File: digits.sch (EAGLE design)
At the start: 49 parts, among them IC1 STP16CP05 / STP16CPC26, IC2 STP16CP05 / STP16CPC26, IC3 ATMEGA32U4QFN, IC4 ATMEGA32U4TQFP-44, J1 POWER_JACKPTH_LOCK, J2 ACCESSORY, X1 CRYSTALHC49

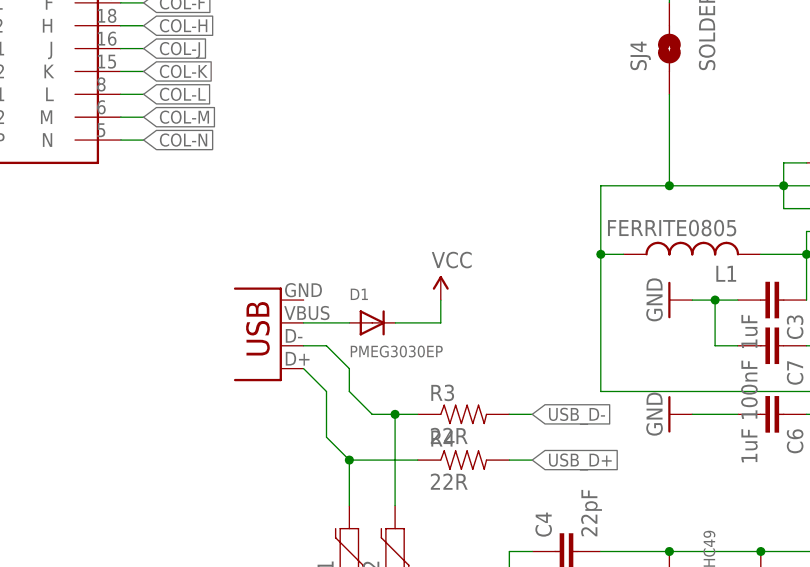
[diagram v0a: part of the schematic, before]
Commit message: grounded usb (fixes #3)
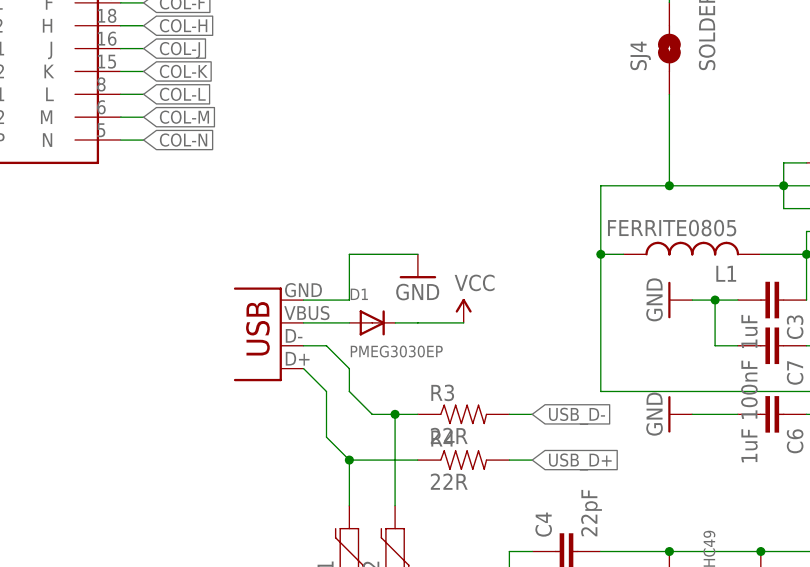
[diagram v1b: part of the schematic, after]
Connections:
- net GND: now also JP2.GND
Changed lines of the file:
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@@
 <attribute name="PARTNO" value="PMEG3030EP-115"/>
 </part>
+<part name="GND17" library="SparkFun-Aesthetics" deviceset="GND" device=""/>
 </parts>
 <sheets>
@@
 <attribute name="PARTNO" x="246.38" y="43.18" size="1.778" layer="96" display="off"/>
 </instance>
-<instance part="SUPPLY3" gate="G$1" x="254" y="45.72"/>
+<instance part="SUPPLY3" gate="G$1" x="256.54" y="43.18"/>
 <instance part="JP3" gate="G$1" x="12.7" y="38.1">
 <attribute name="PARTNO" x="12.7" y="38.1" size="1.778" layer="96" display="off"/>
@@
 <attribute name="PARTNO" x="281.94" y="-40.64" size="1.778" layer="96" display="off"/>
 </instance>
+<instance part="GND17" gate="1" x="251.46" y="48.26"/>
 </instances>
 <busses>
@@
 <pinref part="D1" gate="G$1" pin="C"/>
 <pinref part="SUPPLY3" gate="G$1" pin="VCC"/>
-<wire x1="248.92" y1="43.18" x2="254" y2="43.18" width="0.1524" layer="91"/>
-<wire x1="254" y1="43.18" x2="254" y2="45.72" width="0.1524" layer="91"/>
+<wire x1="248.92" y1="43.18" x2="251.46" y2="43.18" width="0.1524" layer="91"/>
+<wire x1="251.46" y1="43.18" x2="256.54" y2="43.18" width="0.1524" layer="91"/>
 </segment>
 <segment>
@@
 <label x="63.5" y="33.02" size="1.4224" layer="95" xref="yes"/>
 </segment>
-</net>
+<segment>
+<pinref part="JP2" gate="G$1" pin="GND"/>
+<wire x1="238.76" y1="45.72" x2="243.84" y2="45.72" width="0.1524" layer="91"/>
+<wire x1="243.84" y1="45.72" x2="243.84" y2="50.8" width="0.1524" layer="91"/>
+<pinref part="GND17" gate="1" pin="GND"/>
+<wire x1="243.84" y1="50.8" x2="251.46" y2="50.8" width="0.1524" layer="91"/>
+</segment>
+</net>

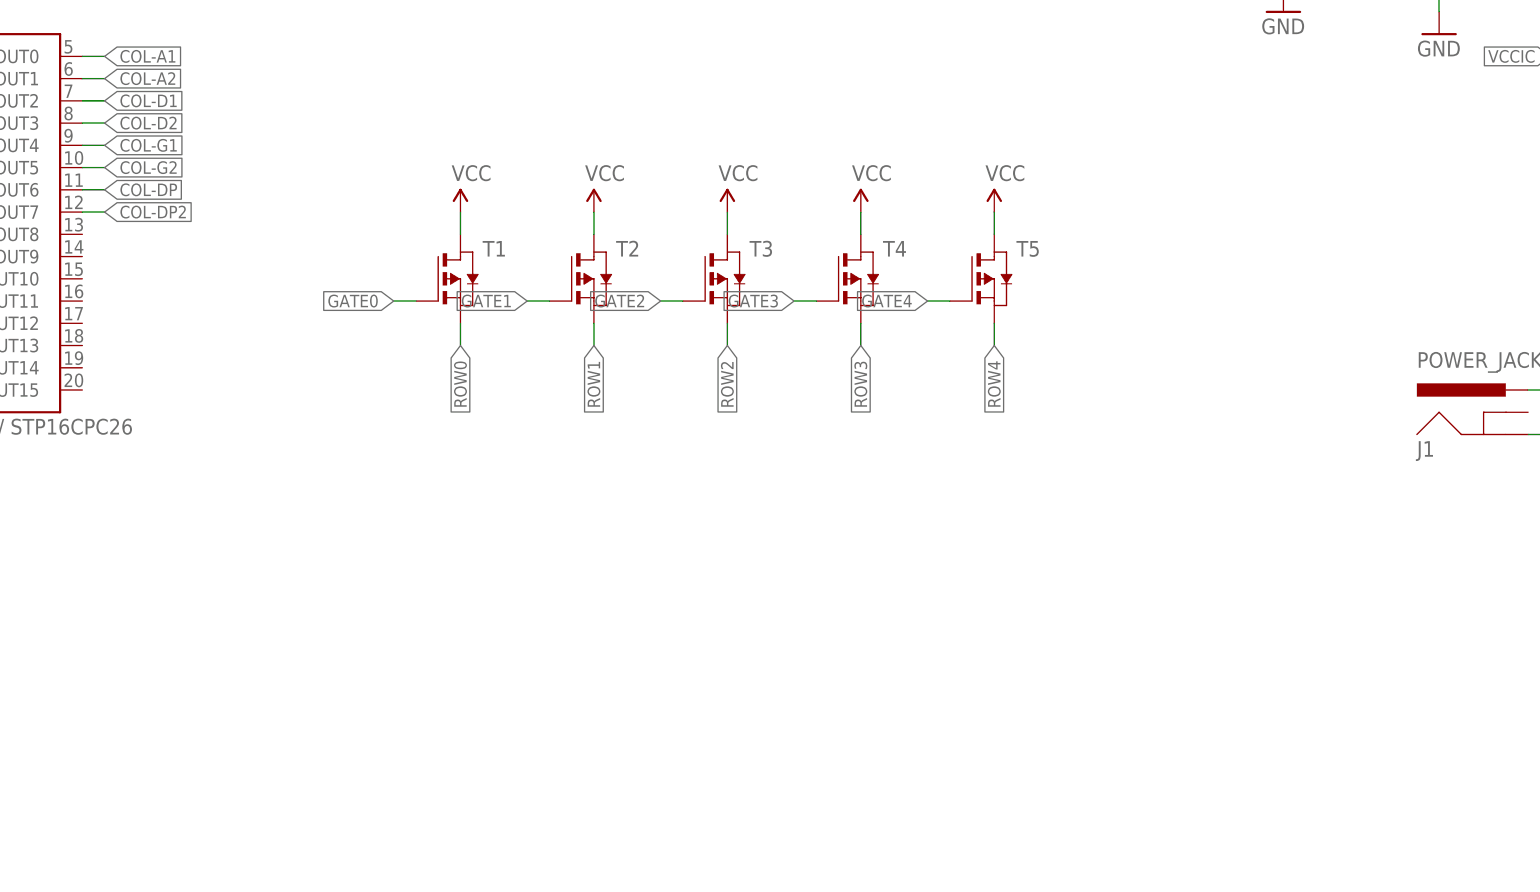
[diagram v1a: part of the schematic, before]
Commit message: increased screw hole size, added resistors, fixed mosfets (fixes #4 fixes #7 fixes #6)
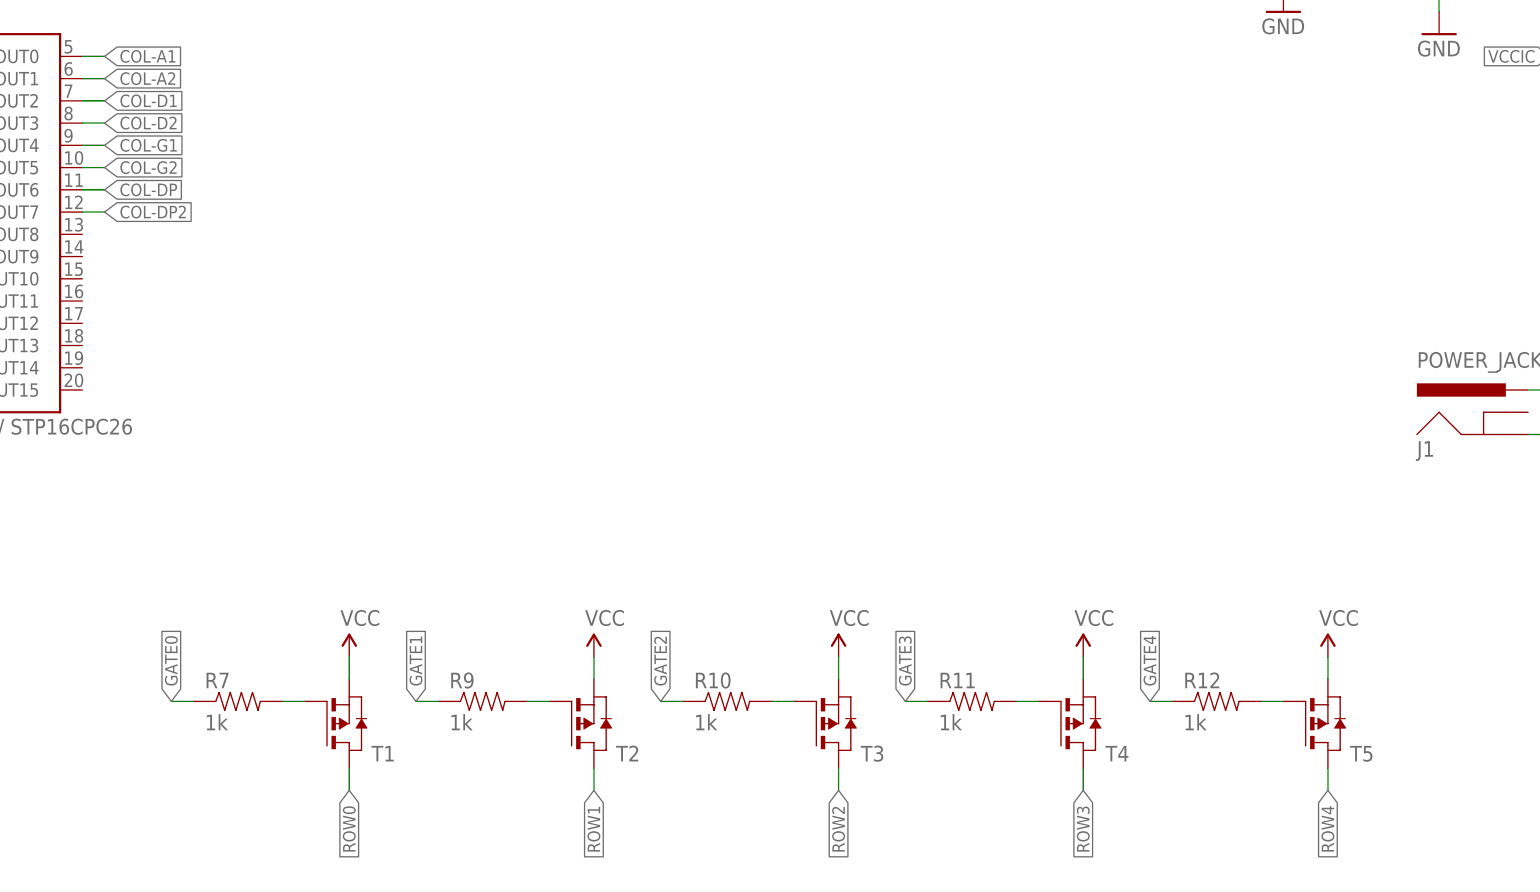
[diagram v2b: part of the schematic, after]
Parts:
- added R10, R11, R12, R7, R9: 1k, SparkFun-Resistors:RESISTOR0805-RES
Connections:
- new net N$10: R9.2, T2.G
- new net N$11: R10.2, T3.G
- new net N$12: R12.2, T5.G
- new net N$8: R11.2, T4.G
- new net N$9: R7.2, T1.G
- net GATE0: now also R7.1; no longer T1.G
- net GATE1: now also R9.1; no longer T2.G
- net GATE2: now also R10.1; no longer T3.G
- net GATE3: now also R11.1; no longer T4.G
- net GATE4: now also R12.1; no longer T5.G
- net ROW0: now also T1.D; no longer T1.S
- net ROW1: now also T2.D; no longer T2.S
- net ROW2: now also T3.D; no longer T3.S
- net ROW3: now also T4.D; no longer T4.S
- net ROW4: now also T5.D; no longer T5.S
- net VCC: now also T1.S, T2.S, T3.S, T4.S, T5.S; no longer T1.D, T2.D, T3.D, T4.D, T5.D
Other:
- moved on the sheet: T1, T2, T3, T4, T5

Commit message: removed adafruit headers, added spark core, reassigning acc pins, reassigning power buses
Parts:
- removed JP4: Adafruit Bluefruit LE, SparkFun-Connectors:M10LOCK
- removed JP5: Adafruit CC3000 Wifi, SparkFun-Connectors:M09LOCK
- removed SJ1, SJ3: SOLDERJUMPERTRACE, SparkFun-Passives:SOLDERJUMPERTRACE
- removed SJ2: SOLDERJUMPERNO, SparkFun-Passives:SOLDERJUMPERNO
- removed SJ4: SOLDERJUMPERTRACE, SparkFun-Retired:SOLDERJUMPERTRACE
- added U$1: SPARK_CORECORE, Spark:SPARK_CORECORE
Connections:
- removed net BF_RDY: JP4.5, SJ1.2, SJ2.2
- removed net MISO: IC3.PB3(MISO), IC4.PB3(MISO), J2.15, JP1.1, JP4.2, JP5.5
- removed net PB0: IC3.PB0(SS), IC4.PB0(SS), J2.18
- removed net PB4: IC3.PB4(ADC11), IC4.PB4(ADC11), J2.10, JP5.8
- removed net PB7: IC3.PB7, IC4.PB7, J2.12, JP4.4
- removed net PC7: IC3.PC7, IC4.PC7, J2.16, JP4.7
- removed net PD2: IC3.PD2(RX), IC4.PD2(RX), J2.5
- removed net PD3: IC3.PD3(TX), IC4.PD3(TX), J2.7
- removed net PD6: IC3.PD6(ADC9), IC4.PD6(ADC9), J2.14, JP4.6
- removed net PD7: IC3.PD7(ADC10), IC4.PD7(ADC10), J2.6, JP5.7
- removed net PE6: IC3.PE6, IC4.PE6, J2.8, SJ1.1, SJ3.1
- removed net PF5: IC3.PF5(ADC5), IC4.PF5(ADC5), J2.24
- removed net PF6: IC3.PF6(ADC6), IC4.PF6(ADC6), J2.22
- removed net PF7: IC3.PF7(ADC7), IC4.PF7(ADC7), J2.20
- removed net PRESENCE: IC3.PE2/!HWB, IC4.PE2/!HWB, J2.23
- removed net VCCIC: C8.1, C9.1, IC3.UVCC, IC3.VBUS, IC3.VCC@14, IC3.VCC@34, IC4.UVCC, IC4.VBUS, IC4.VCC@14, IC4.VCC@34, JP1.2, L1.1, R6.2, SJ4.1
- removed net WIFI_IRQ: JP5.9, SJ3.2
- new net A0: IC3.PF7(ADC7), IC4.PF7(ADC7), J2.20, U$1.A0
- new net A1: IC3.PF6(ADC6), IC4.PF6(ADC6), J2.22, U$1.A1
- new net A2: IC3.PF5(ADC5), IC4.PF5(ADC5), J2.24, U$1.A2
- new net D0/RX: J2.5, U$1.RX
- new net D1/TX: J2.7, U$1.TX
- new net D10: IC3.PD6(ADC9), IC4.PD6(ADC9), J2.12
- new net D11: IC3.PC7, IC4.PC7, J2.14
- new net D12: IC3.PB0(SS), IC4.PB0(SS), J2.16
- new net D13: J2.18
- new net D2/SDA: IC3.PD1(SDA), IC4.PD1(SDA), J2.9, U$1.D0
- new net D3/SCL: IC3.PD0(SCL), IC4.PD0(SCL), J2.11, U$1.D1
- new net D4/MOSI: IC3.PB2(MOSI), IC4.PB2(MOSI), J2.13, JP1.4, U$1.A5
- new net D5/MISO: IC3.PB3(MISO), IC4.PB3(MISO), J2.15, JP1.1, U$1.A4
- new net D6: IC3.PD7(ADC10), IC4.PD7(ADC10)
- new net D6/SCK: IC3.PB1(SCK), IC4.PB1(SCK), J2.17, JP1.3, U$1.A3
- new net D7: IC3.PE6, IC4.PE6, J2.6
- new net D7/PRESENCE: IC3.PE2/!HWB, IC4.PE2/!HWB, J2.23, U$1.D7
- new net D8: IC3.PB4(ADC11), IC4.PB4(ADC11), J2.8
- new net D9: IC3.PB7, IC4.PB7, J2.10
- new net RX: IC3.PD2(RX), IC4.PD2(RX)
- new net TX: IC3.PD3(TX), IC4.PD3(TX)
- new net VCC5V: C8.1, C9.1, D1.C, IC3.UVCC, IC3.VBUS, IC3.VCC@14, IC3.VCC@34, IC4.UVCC, IC4.VBUS, IC4.VCC@14, IC4.VCC@34, JP1.2, L1.1, R6.2, U$1.RAW
- new net VCC9V: D2.C
- net BLANK: now also U$1.A6
- net GATE0: now also U$1.D2
- net GATE1: now also U$1.D3
- net GATE2: now also U$1.D4
- net GATE3: now also U$1.D5
- net GATE4: now also U$1.D6
- net GND: now also U$1.GND@2, U$1.GND@21; no longer JP4.9, JP5.1
- net LATCH: now also U$1.A7
- net MOSI: no longer IC3.PB2(MOSI), IC4.PB2(MOSI), J2.13, JP1.4, JP4.3, JP5.6
- net PD0: no longer IC3.PD0(SCL), IC4.PD0(SCL), J2.11
- net PD1: no longer IC3.PD1(SDA), IC4.PD1(SDA), J2.9, SJ2.1
- net SCK: no longer IC3.PB1(SCK), IC4.PB1(SCK), J2.17, JP1.3, JP4.1, JP5.4
- net VCC: no longer D1.C, D2.C, JP4.10, JP5.3, SJ4.2

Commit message: added boost converter
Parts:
- added C11, C12: 0.1uF, SparkFun-Capacitors:CAP0805
- added C13: 100uF, SparkFun-Capacitors:CAP_POLD
- added C14: 470uF, SparkFun-Capacitors:CAP_POLD
- added C15: 470pF, SparkFun-Capacitors:CAP0805
- added D3: BYV10-40, diode:DIODE-MELF-MLL41
- added IC6: 7805DT, adafruit:7805DT
- added L2: 200uH, Livestream:FERRITESRN1060
- added R13: 0.33R, SparkFun-Resistors:RESISTOR0805-RES
- added R14: 1.2k, SparkFun-Resistors:RESISTOR0805-RES
- added R15: 3.6k, SparkFun-Resistors:RESISTOR0805-RES
- added U1: MC34063SMD, SparkFun-PowerIC:MC34063SMD
- C7, C8, C9: value 100nF -> 0.1uF
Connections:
- removed net D13: J2.18
- removed net MOSI: IC1.SDI, JP3.3
- removed net PD0: JP3.7, JP6.4
- removed net PD1: JP3.8, JP6.3
- removed net SCK: IC1.CLK, IC2.CLK, JP3.4, JP6.7
- new net N$13: R13.1, U1.DVR, U1.SEN, U1.SWC
- new net N$14: D3.C, L2.1, U1.SWE
- new net N$15: C15.2, U1.TC
- new net N$16: R14.2, R15.1, U1.COMP
- new net VCCLEDS: C14.+, L2.2, R15.2, T1.S, T2.S, T3.S, T4.S, T5.S
- net BLANK: no longer JP3.6, JP6.5
- net D0/RX: now also JP3.3, JP6.8
- net D1/TX: now also JP3.4, JP6.7
- net D2/SDA: now also JP3.5, JP6.6
- net D3/SCL: now also JP3.6, JP6.5
- net D4/MOSI: now also IC1.SDI
- net D6/SCK: now also IC1.CLK, IC2.CLK
- net D7: now also JP3.7, JP6.4
- net D8: now also JP3.8, JP6.3
- net GND: now also C11.2, C12.2, C13.-, C14.-, C15.1, D3.A, IC6.GND, R14.1, U1.GND
- net LATCH: no longer JP3.5, JP6.6
- net SDO2: no longer JP6.8
- net VCC: now also C13.+, R13.2, U1.VCC; no longer C1.1, C2.1, IC1.VDD, IC2.VDD, J2.1, J2.2, JP3.1, JP3.2, JP6.10, JP6.9, T1.S, T2.S, T3.S, T4.S, T5.S
- net VCC5V: now also C1.1, C12.1, C2.1, IC1.VDD, IC2.VDD, IC6.VO, J2.1, J2.2, JP3.1, JP6.10
- net VCC9V: now also C11.1, IC6.VI, JP3.2, JP6.9

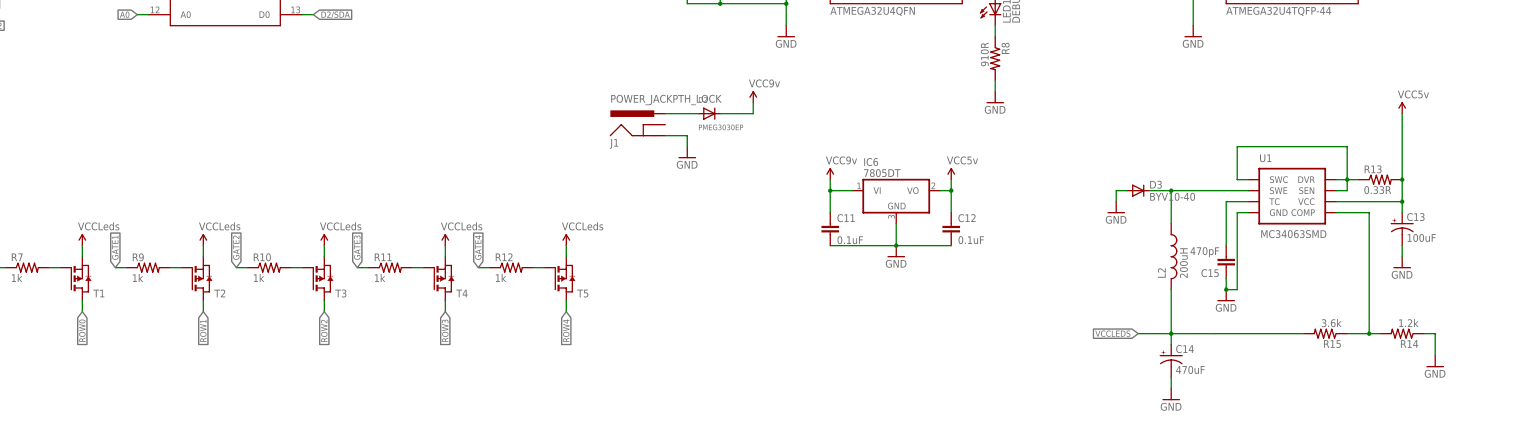
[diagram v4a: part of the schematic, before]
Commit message: added tssop shifter, pololu boost
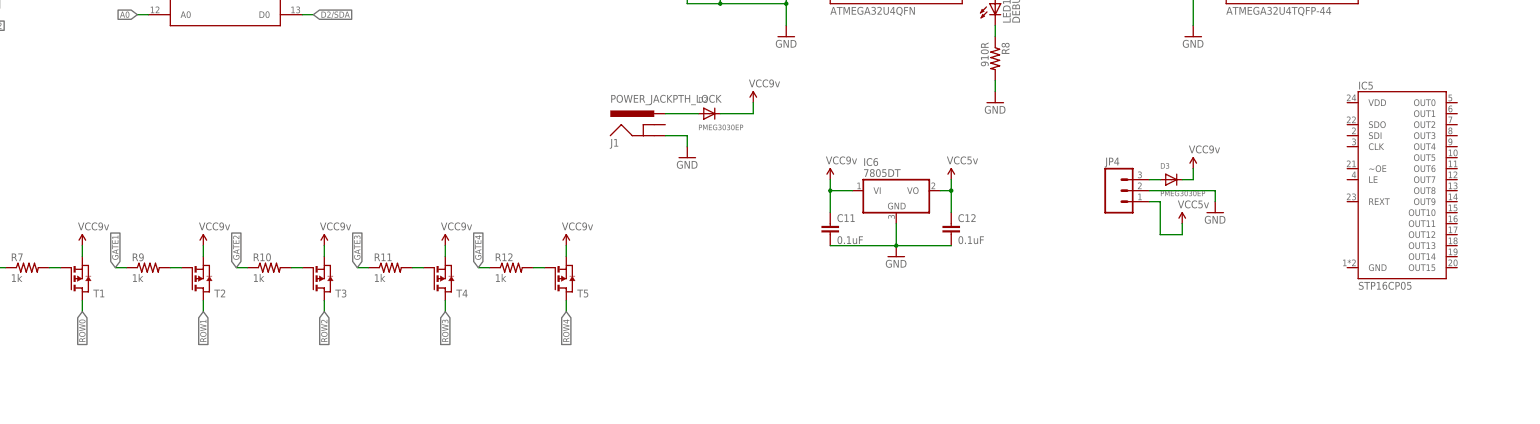
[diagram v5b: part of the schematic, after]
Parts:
- removed C13: 100uF, SparkFun-Capacitors:CAP_POLD
- removed C14: 470uF, SparkFun-Capacitors:CAP_POLD
- removed C15: 470pF, SparkFun-Capacitors:CAP0805
- removed L2: 200uH, Livestream:FERRITESRN1060
- removed R13: 0.33R, SparkFun-Resistors:RESISTOR0805-RES
- removed R14: 1.2k, SparkFun-Resistors:RESISTOR0805-RES
- removed R15: 3.6k, SparkFun-Resistors:RESISTOR0805-RES
- removed U1: MC34063SMD, SparkFun-PowerIC:MC34063SMD
- added IC5: STP16CP05, digits:STP16CP05
- added JP4: (no value), SparkFun-Connectors:M03LOCK
- D3: value BYV10-40 -> PMEG3030EP; device diode:DIODE-MELF-MLL41 -> digits:DIODESOD-128; PARTNO (none) -> PMEG3030EP-115
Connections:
- removed net N$14: D3.C, L2.1, U1.SWE
- removed net N$15: C15.2, U1.TC
- removed net N$16: R14.2, R15.1, U1.COMP
- removed net VCC: C13.+, R13.2, U1.VCC
- removed net VCCLEDS: C14.+, L2.2, R15.2, T1.S, T2.S, T3.S, T4.S, T5.S
- net GND: now also JP4.2; no longer C13.-, C14.-, C15.1, D3.A, R14.1, U1.GND
- net N$13: now also D3.A, JP4.3; no longer R13.1, U1.DVR, U1.SEN, U1.SWC
- net VCC5V: now also JP4.1
- net VCC9V: now also D3.C, T1.S, T2.S, T3.S, T4.S, T5.S
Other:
- moved on the sheet: D3

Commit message: started rerouting
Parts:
- removed IC5: STP16CP05, digits:STP16CP05
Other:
- moved on the sheet: C1, C11, C12, C2, C3, C4, C5, C6, C7, C8, C9, D1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

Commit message: layout, chronodot
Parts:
- added IC5: CHRONODOT, digits:CHRONODOT
- added R13, R14, R15, R16, R17: 910R, SparkFun-Resistors:RESISTOR0805-RES
- added R18: 10k, SparkFun-Resistors:RESISTOR0805-RES
- added SJ1: SOLDERJUMPERNO, SparkFun-Passives:SOLDERJUMPERNO
- R10, R11, R12, R7, R9: value 1k -> 910R
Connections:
- removed net D7/PRESENCE: IC3.PE2/!HWB, IC4.PE2/!HWB, J2.23, U$1.D7
- removed net SDO2: IC2.SDO
- new net N$14: IC5.SQW, R18.2, SJ1.2
- new net PRESENCE: IC3.PE2/!HWB, IC4.PE2/!HWB, J2.23
- net D2/SDA: now also IC5.SDA
- net D3/SCL: now also IC5.SCL
- net D7: now also SJ1.1, U$1.D7
- net GND: now also IC5.GND
- net N$10: now also R14.1
- net N$11: now also R15.1
- net N$12: now also R17.1
- net N$8: now also R16.1
- net N$9: now also R13.1
- net VCC5V: now also IC5.VCC, R18.1
- net VCC9V: now also R13.2, R14.2, R15.2, R16.2, R17.2
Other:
- moved on the sheet: R10, R11, R12, R7, R9

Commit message: more routing fun
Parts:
- added D4, D5: PMEG3030EP, digits:DIODESOD-128
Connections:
- removed net RX: IC3.PD2(RX), IC4.PD2(RX)
- removed net TX: IC3.PD3(TX), IC4.PD3(TX)
- new net N$15: D5.A, U$1.RAW
- net D0/RX: now also IC3.PD2(RX), IC4.PD2(RX)
- net D1/TX: now also IC3.PD3(TX), IC4.PD3(TX)
- net VCC5V: now also D4.A, D4.C, D5.C; no longer U$1.RAW
